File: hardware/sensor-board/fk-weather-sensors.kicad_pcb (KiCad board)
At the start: 2 copper layers, 14.2 x 21.6 mm, 10 parts, among them J1 CONN_01X06, U1 MPL3115A2, U2 TSL2591, U3 SHT31

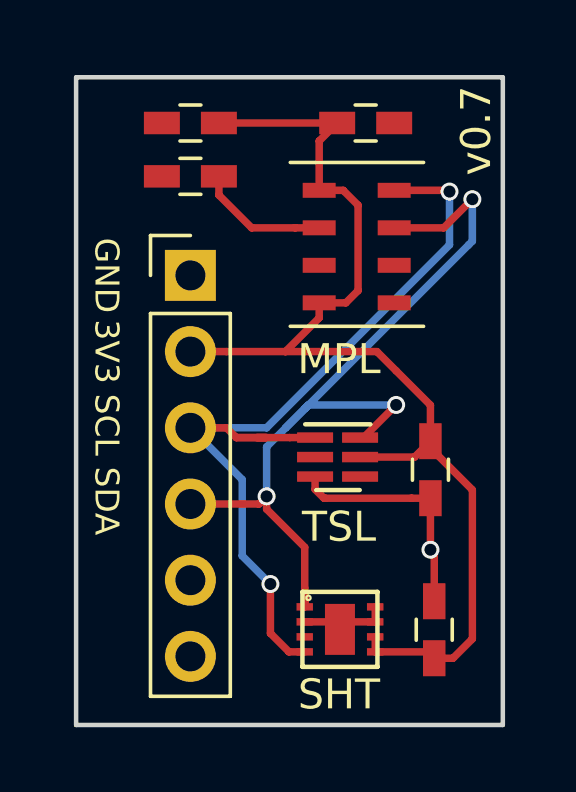
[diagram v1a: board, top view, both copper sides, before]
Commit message: Add RTC. Molex connector cleanup. Add RGB LED.Fix diode footprints.
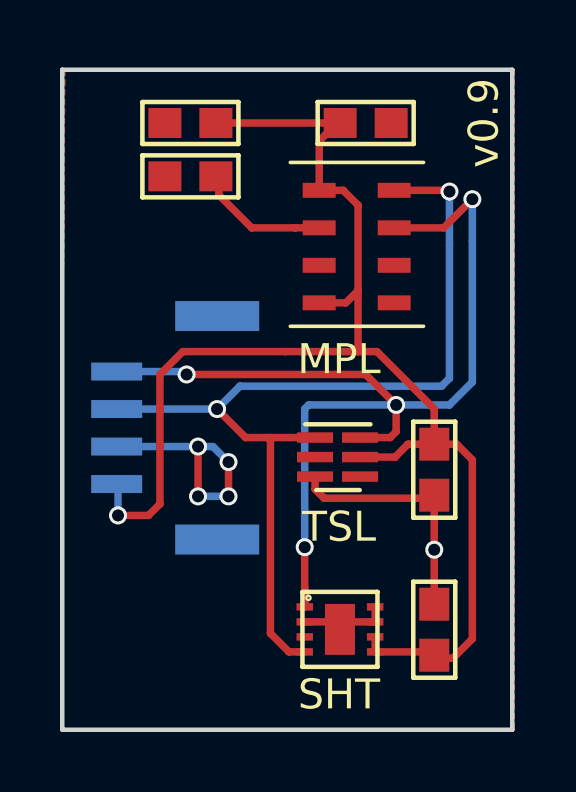
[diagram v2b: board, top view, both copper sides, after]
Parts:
- C1, C2, C3, C4, C5: footprint Capacitors_SMD:C_0603_HandSoldering -> conservify:CAP-0603
- J1: value CONN_01X06 -> CONN_01x04; footprint Socket_Strips:Socket_Strip_Straight_1x06_Pitch2.54mm -> conservify:Molex_CLIK-Mate_502382-0470_1x04_P1.25mm_Vertical; moved to B.Cu
- moved J1 5.11 mm to (144.0, 115.8), turned to 90 degrees
- moved G*** 0.25 mm to (150.4, 115.1)
- moved C3 0.13 mm to (152.7, 117.2)
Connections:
- J1 pad 1: GND -> 3V3
- J1 pad 2: 3V3 -> GND
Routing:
- net 3V3: track 38.1 -> 46.8 mm, vias 0 -> 1
- net GND: track 10.9 -> 18.7 mm, vias 1 -> 5
- net /SDA: track 28.8 -> 34.0 mm, vias 3 -> 4
- net /SCL: track 29.8 -> 31.2 mm
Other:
- board size 14.2 x 21.6 mm -> 15 x 22 mm
- board text added: "15x22mm"
- board text added: "v0.9"
- board text removed: "3V3"
- board text removed: "GND"
- board text removed: "SCL"
- board text removed: "SDA"
- board text removed: "v0.7"

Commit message: Bump version and plot gerbers.
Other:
- board text added: "v0.10"
- board text removed: "v0.9"
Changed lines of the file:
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@@
     (effects (font (size 1.5 1.5) (thickness 0.3)))
   )
-  (gr_text v0.9 (at 154.305 105.664 90) (layer F.SilkS)
+  (gr_text v0.10 (at 154.2669 106.2863 90) (layer F.SilkS)
     (effects (font (size 1 1) (thickness 0.15)))
   )
